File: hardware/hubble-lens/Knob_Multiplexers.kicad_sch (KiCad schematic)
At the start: 25 parts

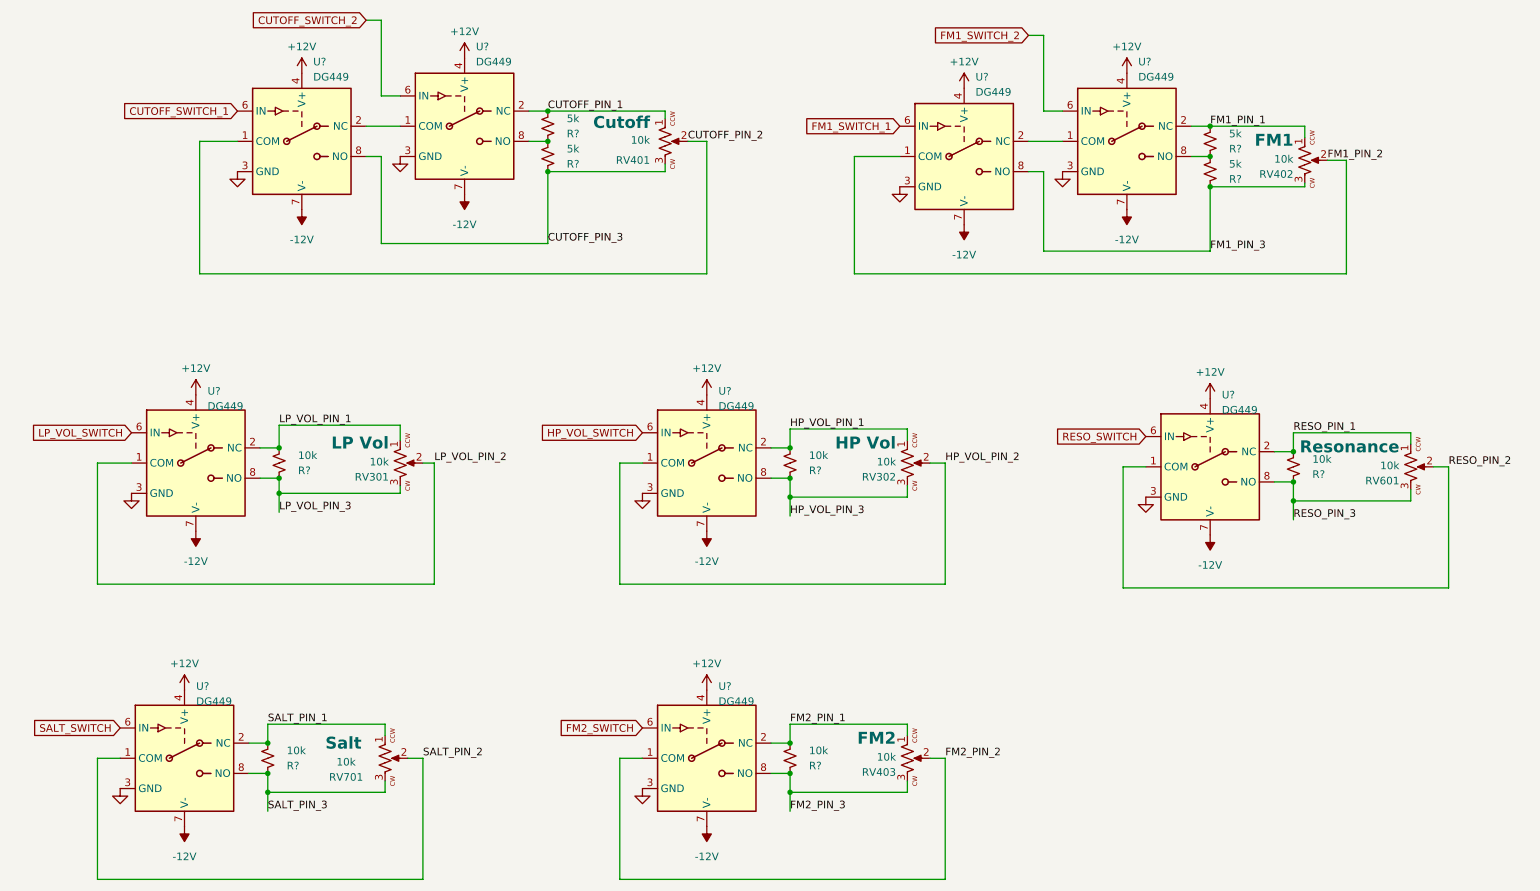
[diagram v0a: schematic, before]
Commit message: update hubble-lens to kicad 9
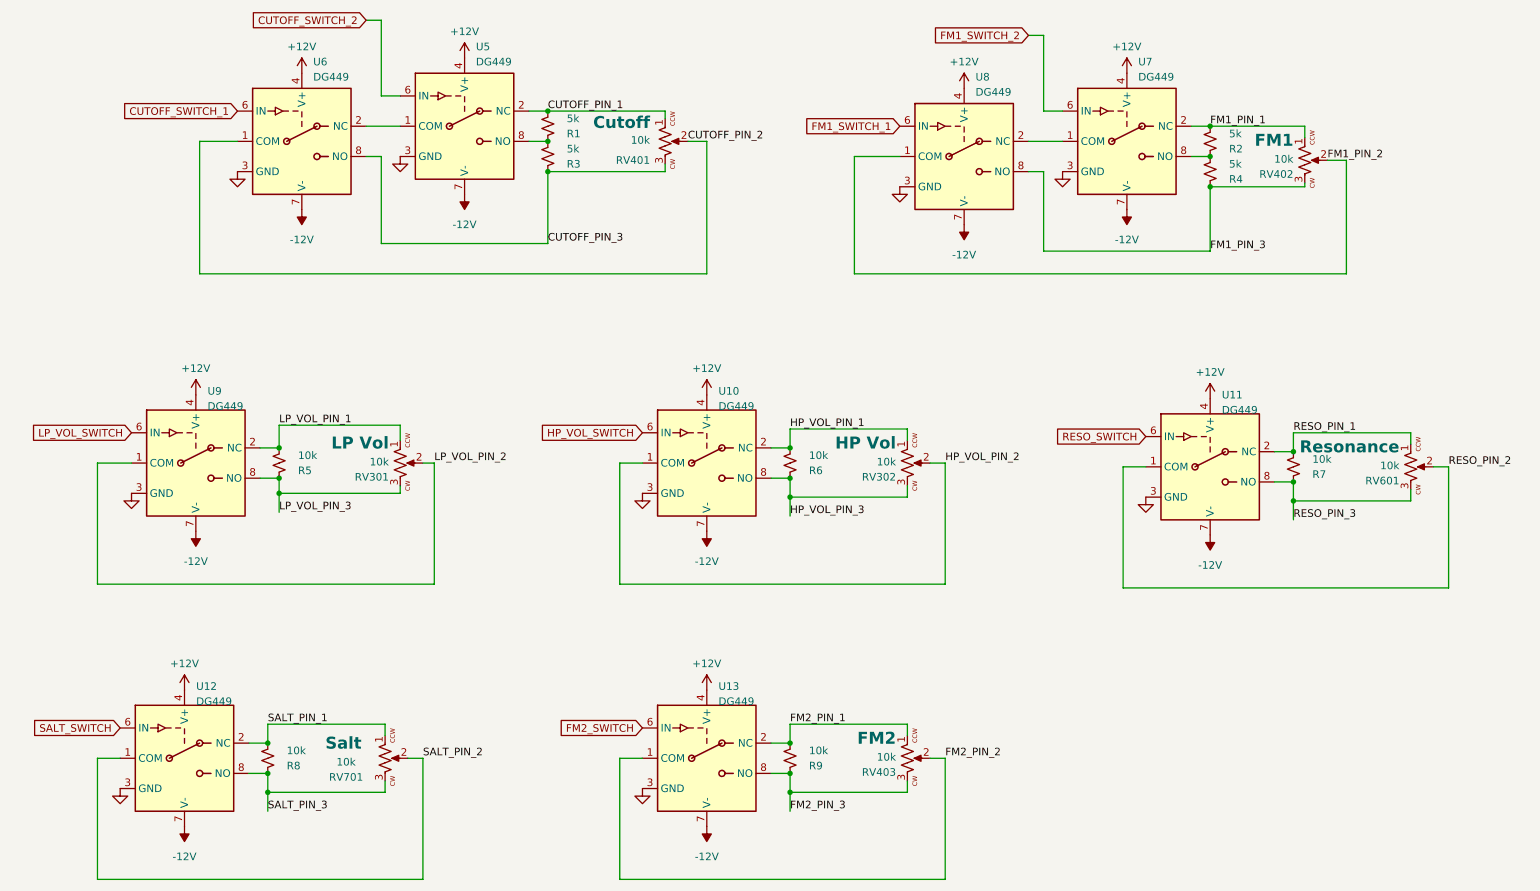
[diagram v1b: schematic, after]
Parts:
- gave numbers to parts that had none: 18
